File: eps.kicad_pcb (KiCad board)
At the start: 4 copper layers, 95.9 x 90.2 mm, 186 parts, among them J1 PC104-8BIT, J2 PC104PTH, J3 PC104PTH, J4 PC104PTH, J5 PC104PTH, P1 3pin-DC-power, P2 3pin-DC-power, Q10 CSD17551Q3A, Q11 CSD17551Q3A, Q12 CSD17551Q3A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

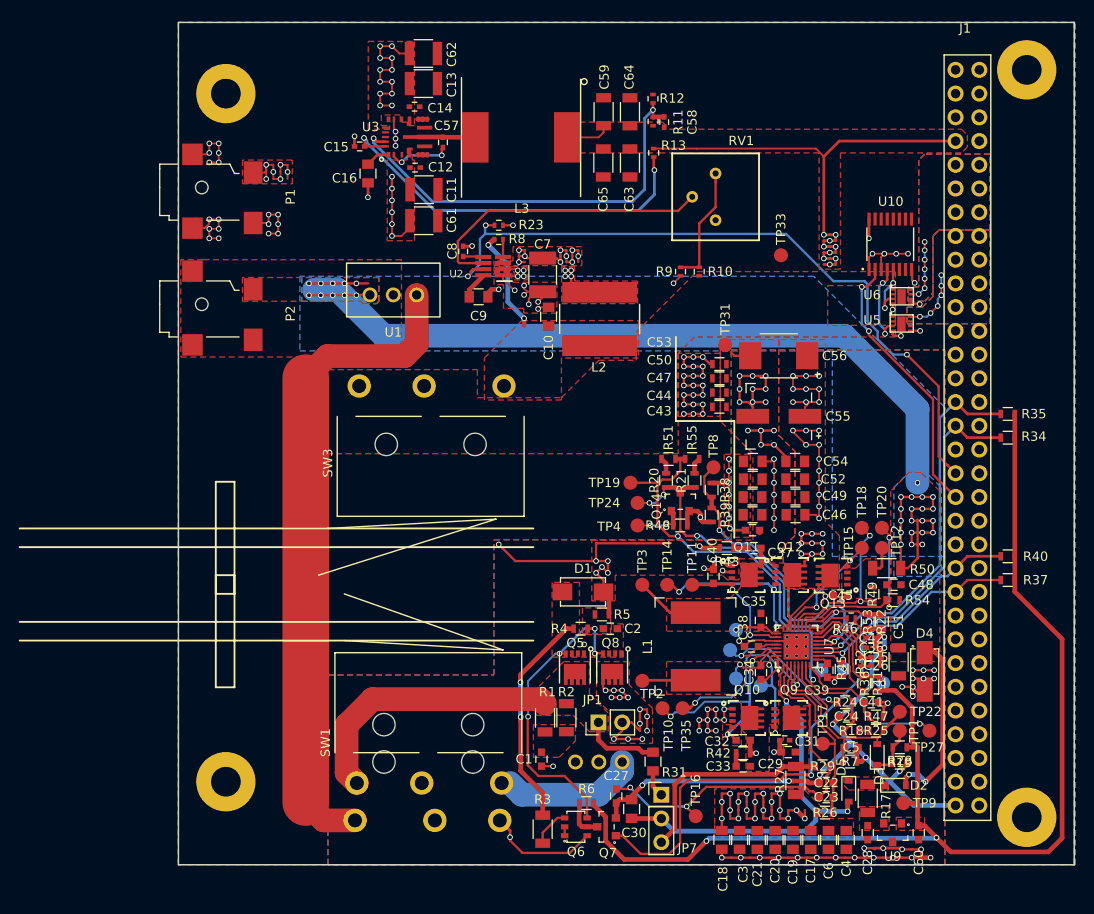
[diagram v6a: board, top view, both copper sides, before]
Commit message: simplified polygons, added holes for pin guides, added testpoints for power nets
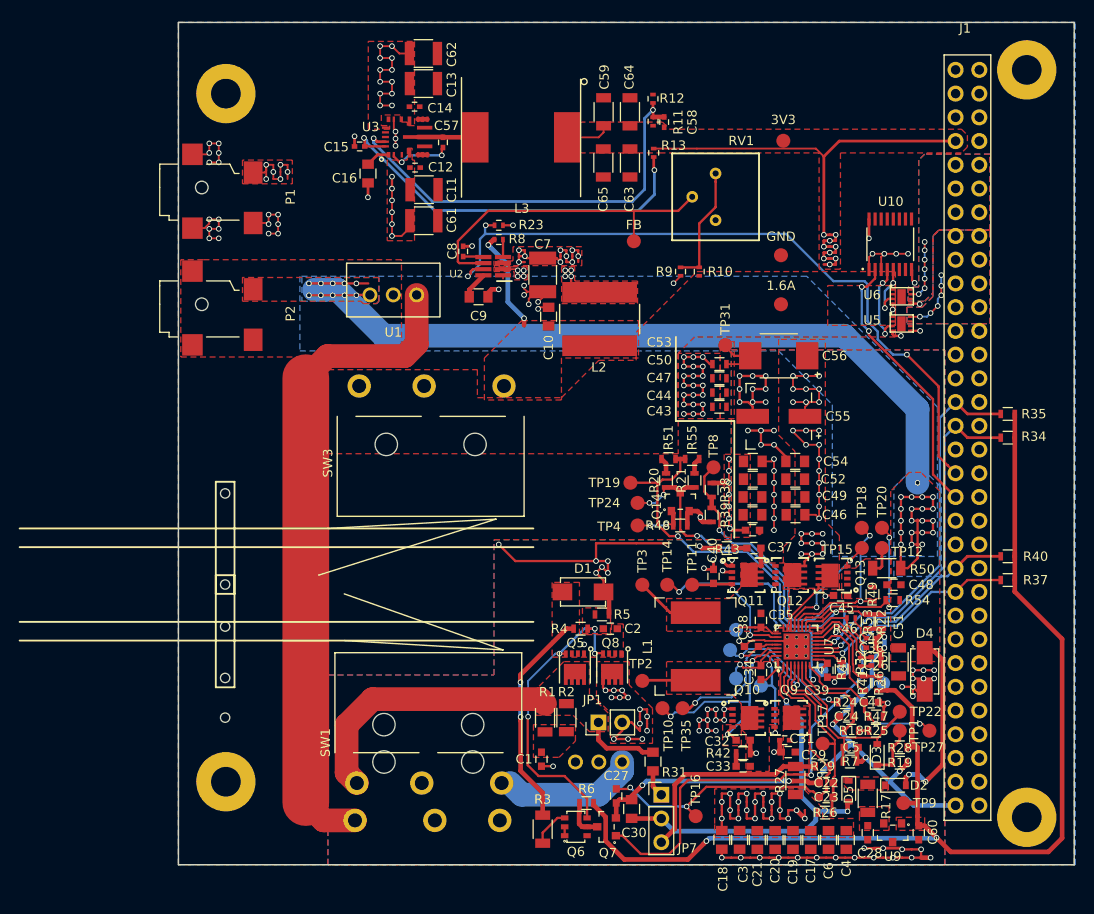
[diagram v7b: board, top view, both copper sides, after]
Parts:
- added REF**: NPTH-1mm, SFUSat:NPTH-1mm, F.Cu at (110.0, 109.5)
- added REF**: NPTH-1mm, SFUSat:NPTH-1mm, F.Cu at (110.0, 119.2)
- added REF**: NPTH-1mm, SFUSat:NPTH-1mm, F.Cu at (110.0, 95.2)
- added REF**: NPTH-1mm, SFUSat:NPTH-1mm, F.Cu at (110.0, 105.0)
- added REF**: NPTH-1mm, SFUSat:NPTH-1mm, F.Cu at (110.0, 115.0)
- added TP23: TEST, SFUSat:Measurement_Point_Round-SMD-Pad_Small, F.Cu at (153.8, 68.2)
- added TP25: TEST, SFUSat:Measurement_Point_Round-SMD-Pad_Small, F.Cu at (169.5, 75.0)
- added TP28: TEST, SFUSat:Measurement_Point_Round-SMD-Pad_Small, F.Cu at (169.8, 57.5)
- SW1: footprint SS-3GLPD-L -> SFUSat:SS-3GLPD-L
- SW3: footprint SS-3GLPD-R -> SFUSat:SS-3GLPD-R
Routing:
- net GNDPWR: track 153.5 -> 145.3 mm, vias 76 -> 75
- net /FB: track 32.0 -> 35.3 mm
- net GND: track 154.4 -> 152.6 mm, vias 69 -> 68
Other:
- board text added: "1.6A"
- board text added: "3V3"
- board text added: "FB"
- board text added: "GND"

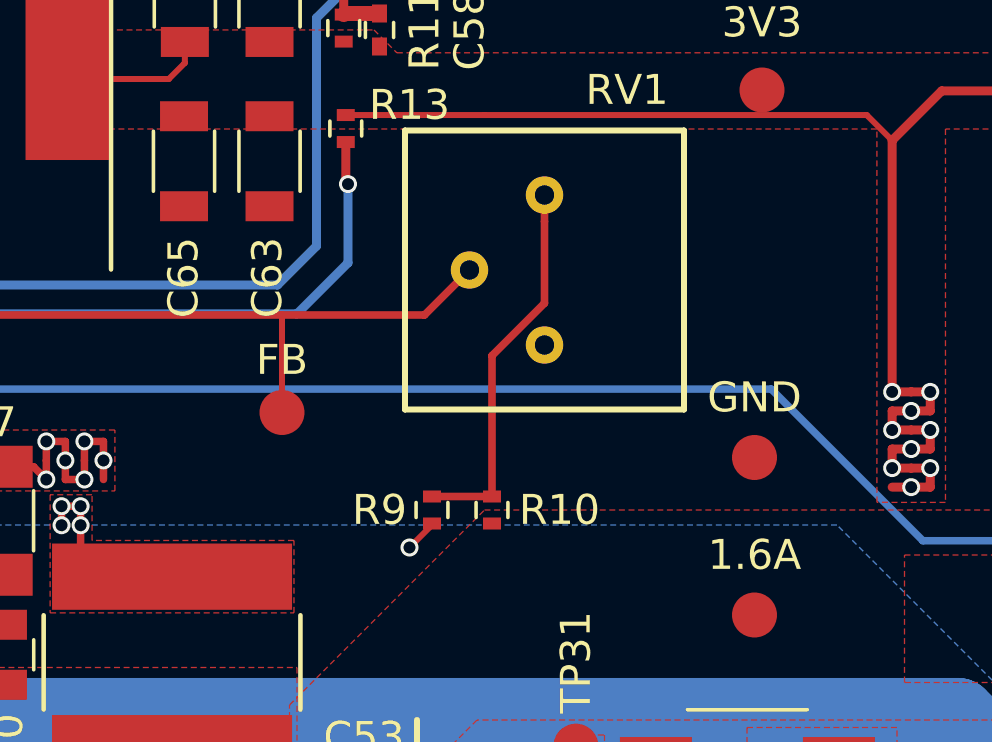
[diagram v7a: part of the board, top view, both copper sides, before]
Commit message: modified FB pot config
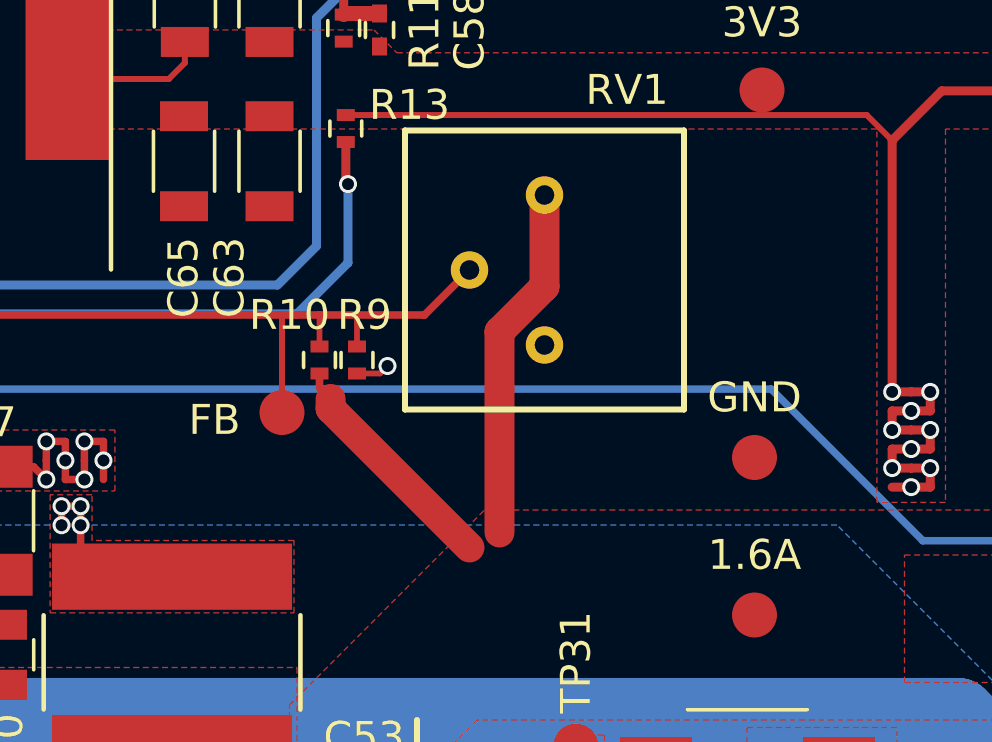
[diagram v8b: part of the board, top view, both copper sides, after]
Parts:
- R10: value 73k2 -> 1k62
- moved R10 6.73 mm to (156.2, 66.5), turned to 270 degrees
- moved R9 6.25 mm to (155.0, 66.5), turned to 90 degrees
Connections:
- R10 pad 1: /PowerDistributionDeploymentControl/1.6A -> /FB
- R10 pad 2: Net-(R10-Pad2) -> GND
- R9 pad 1: Net-(R10-Pad2) -> /PowerDistributionDeploymentControl/1.6A
- R9 pad 2: GND -> /FB
- RV1 pad 1: Net-(R10-Pad2) -> /PowerDistributionDeploymentControl/1.6A
- RV1 pad 3: GND -> Net-(RV1-Pad3)
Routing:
- net /PowerDistributionDeploymentControl/1.6A: track 0.00 -> 19.7 mm
- net Net-(R10-Pad2): track 12.8 -> 0.00 mm
- net /FB: track 35.3 -> 37.4 mm
